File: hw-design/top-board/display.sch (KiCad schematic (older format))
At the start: 0 parts

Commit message: sch,top-board: added glcd
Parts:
- added C? (x18): 1uF, symbol C
- added C? (x2): 100nF, symbol C
- added C? (x2): 10uF, symbol CP
- added DS? (x2): ERC12864-2, symbol ERC12864-2
- added P? (x2): BACKLIGHT, symbol CONN_01X02
- added Q? (x2): 2N7002, symbol Q_NMOS_GSD
- added R? (x2): 100K, symbol R
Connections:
- new net: C?.1, DS?.10 (CAP2-) (x2)
- new net: C?.2, DS?.11 (CAP2+) (x2)
- new net: C?.1, DS?.12 (CAP1+) (x2)
- new net: C?.2, C?.2, DS?.13 (CAP1-) (x2)
- new net: C?.1, DS?.14 (CAP3+) (x2)
- new net: C?.2, DS?.15 (VOUT) (x2)
- new net: C?.2, DS?.6 (V4) (x2)
- new net: C?.2, DS?.7 (V3) (x2)
- new net: C?.2, DS?.8 (V2) (x2)
- new net: C?.2, DS?.9 (V1) (x2)
- new net: C?.2, DS?.5 (V0) (x2)
- new net: P?.1 (P1), Q?.3 (D), R?.1 (x2)
- new net +3V3: C?.1, C?.1, C?.1, C?.1, DS?.1 (IRS), DS?.1 (IRS), DS?.17 (VDD), DS?.17 (VDD), DS?.20 (DB5), DS?.20 (DB5), DS?.21 (DB4), DS?.21 (DB4), DS?.22 (DB3), DS?.22 (DB3), DS?.23 (DB2), DS?.23 (DB2), DS?.24 (DB1), DS?.24 (DB1), DS?.25 (DB0), DS?.25 (DB0), DS?.26 (~RD~(E)), DS?.26 (~RD~(E)), DS?.27 (~WR~(R~W~)), DS?.27 (~WR~(R~W~)), P?.2 (P2), P?.2 (P2), R?.2, R?.2
- new net GLCD1_BL: Q?.1 (G)
- new net GLCD1_CS: DS?.30 (~CS~)
- new net GLCD2_BL: Q?.1 (G)
- new net GLCD2_CS: DS?.30 (~CS~)
- new net GLCD_A0: DS?.28 (A0), DS?.28 (A0)
- new net GLCD_RESET: DS?.29 (~RES~), DS?.29 (~RES~)
- new net GLCD_SCL: DS?.19 (DB6(SCL)), DS?.19 (DB6(SCL))
- new net GLCD_SI: DS?.18 (DB7(SI)), DS?.18 (DB7(SI))
- new net GNDD: C?.1, C?.1, C?.1, C?.1, C?.1, C?.1, C?.1, C?.1, C?.1, C?.1, C?.1, C?.1, C?.2, C?.2, C?.2, C?.2, DS?.16 (VSS), DS?.16 (VSS), DS?.2 (P/~S~), DS?.2 (P/~S~), DS?.3 (C86), DS?.3 (C86), Q?.2 (S), Q?.2 (S)
- no-connect marks 0 -> 2

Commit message: sch,top-board: annotation done
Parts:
- gave numbers to parts that had none: 30

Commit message: sch,top-board: DRC passing
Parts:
- added R2, R4: 100R, symbol R
- renumbered R2 to R3
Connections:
- net +3V3: now also R2.2, R4.2; no longer DS1.20 (DB5), DS1.21 (DB4), DS1.22 (DB3), DS1.23 (DB2), DS1.24 (DB1), DS1.25 (DB0), DS1.26 (~RD~(E)), DS1.27 (~WR~(R~W~)), DS2.20 (DB5), DS2.21 (DB4), DS2.22 (DB3), DS2.23 (DB2), DS2.24 (DB1), DS2.25 (DB0), DS2.26 (~RD~(E)), DS2.27 (~WR~(R~W~))
- new net: DS2.20 (DB5), DS2.21 (DB4), DS2.22 (DB3), DS2.23 (DB2), DS2.24 (DB1), DS2.25 (DB0), DS2.26 (~RD~(E)), DS2.27 (~WR~(R~W~)), R4.1
- new net: DS1.20 (DB5), DS1.21 (DB4), DS1.22 (DB3), DS1.23 (DB2), DS1.24 (DB1), DS1.25 (DB0), DS1.26 (~RD~(E)), DS1.27 (~WR~(R~W~)), R2.1

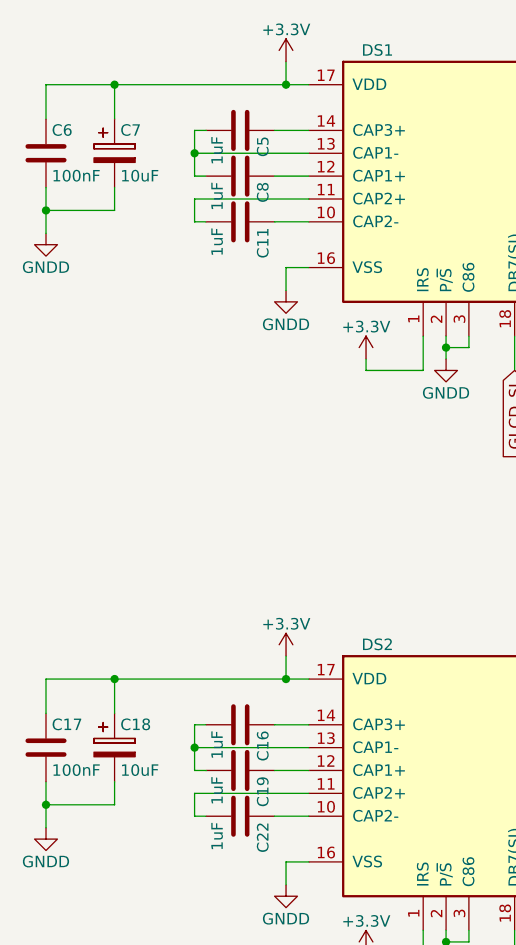
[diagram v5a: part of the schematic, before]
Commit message: sch,top-board: BOM added
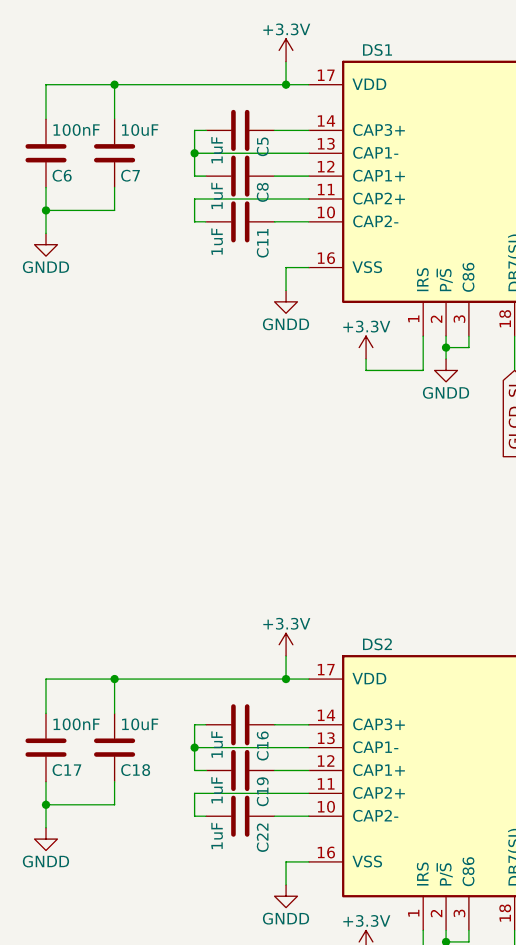
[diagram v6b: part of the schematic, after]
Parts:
- removed C18, C7: 10uF, symbol CP
- added C18, C7: 10uF, symbol C
- C10, C11, C12, C13, C14, C15, C16, C19, C20, C21, C22, C23, C24, C25, C26, C5, C8, C9: MPN (none) -> C2012X7R1E105K125AB
- C17, C6: MPN (none) -> C1608X7R1E104K080AA
- DS1, DS2: MPN (none) -> ERC12864FSF-2
- Q1, Q2: MPN (none) -> 2N7002P,215
- R1, R3: MPN (none) -> RMCF0603JT100K
- R2, R4: MPN (none) -> RMCF0603JT100R
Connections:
- net +3V3: now also C17.2, C6.2, C18.2, C7.2; no longer C17.1, C6.1
- net GNDD: now also C17.1, C6.1, C18.1, C7.1; no longer C17.2, C6.2

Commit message: sch,top-board: footprints creation/assignment done
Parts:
- C10, C11, C12, C13, C14, C15, C16, C18, C19, C20, C21, C22, C23, C24, C25, C26, C5, C7, C8, C9: footprint (none) -> Capacitors_SMD:C_0805
- C17, C6: footprint (none) -> Capacitors_SMD:C_0603
- DS1, DS2: footprint (none) -> footprints:ER-CON30HB-1
- P2: footprint (none) -> footprints:SMD_Pin_Header_Angled_2x01_Pitch2mm; MPN (none) -> ER-CON2.0-2P-SMD
- P3: MPN (none) -> footprints:SMD_Pin_Header_Angled_2x01_Pitch2mm
- Q1, Q2: footprint (none) -> Housings_SOT-23_SOT-143_TSOT-6:SOT-23
- R1, R2, R3, R4: footprint (none) -> Resistors_SMD:R_0603
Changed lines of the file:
@@
 F 0 "DS1" H 4200 2250 50  0000 C CNN
 F 1 "ERC12864-2" H 5200 2250 50  0000 C CNN
-F 2 "" H 5200 2250 50  0000 C CIN
+F 2 "footprints:ER-CON30HB-1" H 5200 2250 50  0001 C CIN
 F 3 "" H 5200 1600 60  0000 C CNN
 F 4 "ERC12864FSF-2" H 0   0   50  0001 C CNN "MPN"
@@
 F 0 "C11" H 3625 2000 50  0000 L CNN
 F 1 "1uF" H 3625 1800 50  0000 L CNN
-F 2 "" H 3638 1750 30  0000 C CNN
+F 2 "Capacitors_SMD:C_0805" H 3638 1750 30  0001 C CNN
 F 3 "" H 3600 1900 60  0000 C CNN
 F 4 "C2012X7R1E105K125AB" H 0   0   50  0001 C CNN "MPN"
@@
 F 0 "C8" H 3625 1800 50  0000 L CNN
 F 1 "1uF" H 3625 1600 50  0000 L CNN
-F 2 "" H 3638 1550 30  0000 C CNN
+F 2 "Capacitors_SMD:C_0805" H 3638 1550 30  0001 C CNN
 F 3 "" H 3600 1700 60  0000 C CNN
 F 4 "C2012X7R1E105K125AB" H 0   0   50  0001 C CNN "MPN"
@@
 F 0 "C5" H 3625 1600 50  0000 L CNN
 F 1 "1uF" H 3625 1400 50  0000 L CNN
-F 2 "" H 3638 1350 30  0000 C CNN
+F 2 "Capacitors_SMD:C_0805" H 3638 1350 30  0001 C CNN
 F 3 "" H 3600 1500 60  0000 C CNN
 F 4 "C2012X7R1E105K125AB" H 0   0   50  0001 C CNN "MPN"
@@
 F 0 "C15" H 6500 2300 50  0000 L CNN
 F 1 "1uF" H 6625 2100 50  0000 L CNN
-F 2 "" H 6638 2050 30  0000 C CNN
+F 2 "Capacitors_SMD:C_0805" H 6638 2050 30  0001 C CNN
 F 3 "" H 6600 2200 60  0000 C CNN
 F 4 "C2012X7R1E105K125AB" H 0   0   50  0001 C CNN "MPN"
@@
 F 0 "C14" H 6700 2200 50  0000 L CNN
 F 1 "1uF" H 6825 2000 50  0000 L CNN
-F 2 "" H 6838 1950 30  0000 C CNN
+F 2 "Capacitors_SMD:C_0805" H 6838 1950 30  0001 C CNN
 F 3 "" H 6800 2100 60  0000 C CNN
 F 4 "C2012X7R1E105K125AB" H 0   0   50  0001 C CNN "MPN"
@@
 F 0 "C13" H 6900 2100 50  0000 L CNN
 F 1 "1uF" H 7025 1900 50  0000 L CNN
-F 2 "" H 7038 1850 30  0000 C CNN
+F 2 "Capacitors_SMD:C_0805" H 7038 1850 30  0001 C CNN
 F 3 "" H 7000 2000 60  0000 C CNN
 F 4 "C2012X7R1E105K125AB" H 0   0   50  0001 C CNN "MPN"
@@
 F 0 "C12" H 7100 2000 50  0000 L CNN
 F 1 "1uF" H 7225 1800 50  0000 L CNN
-F 2 "" H 7238 1750 30  0000 C CNN
+F 2 "Capacitors_SMD:C_0805" H 7238 1750 30  0001 C CNN
 F 3 "" H 7200 1900 60  0000 C CNN
 F 4 "C2012X7R1E105K125AB" H 0   0   50  0001 C CNN "MPN"
@@
 F 0 "C10" H 7300 1900 50  0000 L CNN
 F 1 "1uF" H 7425 1700 50  0000 L CNN
-F 2 "" H 7438 1650 30  0000 C CNN
+F 2 "Capacitors_SMD:C_0805" H 7438 1650 30  0001 C CNN
 F 3 "" H 7400 1800 60  0000 C CNN
 F 4 "C2012X7R1E105K125AB" H 0   0   50  0001 C CNN "MPN"
@@
 F 0 "C9" H 7500 1800 50  0000 L CNN
 F 1 "1uF" H 7625 1600 50  0000 L CNN
-F 2 "" H 7638 1550 30  0000 C CNN
+F 2 "Capacitors_SMD:C_0805" H 7638 1550 30  0001 C CNN
 F 3 "" H 7600 1700 60  0000 C CNN
 F 4 "C2012X7R1E105K125AB" H 0   0   50  0001 C CNN "MPN"
@@
 F 0 "C6" H 2775 1700 50  0000 L CNN
 F 1 "100nF" H 2775 1500 50  0000 L CNN
-F 2 "" H 2788 1450 30  0000 C CNN
+F 2 "Capacitors_SMD:C_0603" H 2788 1450 30  0001 C CNN
 F 3 "" H 2750 1600 60  0000 C CNN
 F 4 "C1608X7R1E104K080AA" H 0   0   50  0001 C CNN "MPN"
@@
 F 0 "DS2" H 4200 4850 50  0000 C CNN
 F 1 "ERC12864-2" H 5200 4850 50  0000 C CNN
-F 2 "" H 5200 4850 50  0000 C CIN
+F 2 "footprints:ER-CON30HB-1" H 5200 4850 50  0001 C CIN
 F 3 "" H 5200 4200 60  0000 C CNN
 F 4 "ERC12864FSF-2" H 0   0   50  0001 C CNN "MPN"
@@
 F 0 "C22" H 3625 4600 50  0000 L CNN
 F 1 "1uF" H 3625 4400 50  0000 L CNN
-F 2 "" H 3638 4350 30  0000 C CNN
+F 2 "Capacitors_SMD:C_0805" H 3638 4350 30  0001 C CNN
 F 3 "" H 3600 4500 60  0000 C CNN
 F 4 "C2012X7R1E105K125AB" H 0   0   50  0001 C CNN "MPN"
@@
 F 0 "C19" H 3625 4400 50  0000 L CNN
 F 1 "1uF" H 3625 4200 50  0000 L CNN
-F 2 "" H 3638 4150 30  0000 C CNN
+F 2 "Capacitors_SMD:C_0805" H 3638 4150 30  0001 C CNN
 F 3 "" H 3600 4300 60  0000 C CNN
 F 4 "C2012X7R1E105K125AB" H 0   0   50  0001 C CNN "MPN"
@@
 F 0 "C16" H 3625 4200 50  0000 L CNN
 F 1 "1uF" H 3625 4000 50  0000 L CNN
-F 2 "" H 3638 3950 30  0000 C CNN
+F 2 "Capacitors_SMD:C_0805" H 3638 3950 30  0001 C CNN
 F 3 "" H 3600 4100 60  0000 C CNN
 F 4 "C2012X7R1E105K125AB" H 0   0   50  0001 C CNN "MPN"
@@
 F 0 "C26" H 6500 4900 50  0000 L CNN
 F 1 "1uF" H 6625 4700 50  0000 L CNN
-F 2 "" H 6638 4650 30  0000 C CNN
+F 2 "Capacitors_SMD:C_0805" H 6638 4650 30  0001 C CNN
 F 3 "" H 6600 4800 60  0000 C CNN
 F 4 "C2012X7R1E105K125AB" H 0   0   50  0001 C CNN "MPN"
@@
 F 0 "C25" H 6700 4800 50  0000 L CNN
 F 1 "1uF" H 6825 4600 50  0000 L CNN
-F 2 "" H 6838 4550 30  0000 C CNN
+F 2 "Capacitors_SMD:C_0805" H 6838 4550 30  0001 C CNN
 F 3 "" H 6800 4700 60  0000 C CNN
 F 4 "C2012X7R1E105K125AB" H 0   0   50  0001 C CNN "MPN"
@@
 F 0 "C24" H 6900 4700 50  0000 L CNN
 F 1 "1uF" H 7025 4500 50  0000 L CNN
-F 2 "" H 7038 4450 30  0000 C CNN
+F 2 "Capacitors_SMD:C_0805" H 7038 4450 30  0001 C CNN
 F 3 "" H 7000 4600 60  0000 C CNN
 F 4 "C2012X7R1E105K125AB" H 0   0   50  0001 C CNN "MPN"
@@
 F 0 "C23" H 7100 4600 50  0000 L CNN
 F 1 "1uF" H 7225 4400 50  0000 L CNN
-F 2 "" H 7238 4350 30  0000 C CNN
+F 2 "Capacitors_SMD:C_0805" H 7238 4350 30  0001 C CNN
 F 3 "" H 7200 4500 60  0000 C CNN
 F 4 "C2012X7R1E105K125AB" H 0   0   50  0001 C CNN "MPN"
@@
 F 0 "C21" H 7300 4500 50  0000 L CNN
 F 1 "1uF" H 7425 4300 50  0000 L CNN
-F 2 "" H 7438 4250 30  0000 C CNN
+F 2 "Capacitors_SMD:C_0805" H 7438 4250 30  0001 C CNN
 F 3 "" H 7400 4400 60  0000 C CNN
 F 4 "C2012X7R1E105K125AB" H 0   0   50  0001 C CNN "MPN"
@@
 F 0 "C20" H 7500 4400 50  0000 L CNN
 F 1 "1uF" H 7625 4200 50  0000 L CNN
-F 2 "" H 7638 4150 30  0000 C CNN
+F 2 "Capacitors_SMD:C_0805" H 7638 4150 30  0001 C CNN
 F 3 "" H 7600 4300 60  0000 C CNN
 F 4 "C2012X7R1E105K125AB" H 0   0   50  0001 C CNN "MPN"
@@
 F 0 "P2" H 9250 1550 50  0000 C CNN
 F 1 "BACKLIGHT" V 9350 1400 50  0000 C CNN
-F 2 "" H 9250 1400 60  0000 C CNN
+F 2 "footprints:SMD_Pin_Header_Angled_2x01_Pitch2mm" H 9250 1400 60  0001 C CNN
 F 3 "" H 9250 1400 60  0000 C CNN
+F 4 "ER-CON2.0-2P-SMD" H 9250 1400 60  0001 C CNN "MPN"
 	1    9250 1400
 	0    -1   -1   0
@@
 F 0 "R1" V 8980 1500 50  0000 C CNN
 F 1 "100K" V 8900 1500 50  0000 C CNN
-F 2 "" V 8830 1500 30  0000 C CNN
+F 2 "Resistors_SMD:R_0603" V 8830 1500 30  0001 C CNN
 F 3 "" H 8900 1500 30  0000 C CNN
 F 4 "RMCF0603JT100K" H 0   0   50  0001 C CNN "MPN"
@@
 F 0 "P3" H 9250 4150 50  0000 C CNN
 F 1 "BACKLIGHT" V 9350 4000 50  0000 C CNN
-F 2 "" H 9250 4000 60  0000 C CNN
+F 2 "" H 9250 4000 60  0001 C CNN
 F 3 "" H 9250 4000 60  0000 C CNN
+F 4 "ER-CON2.0-2P-SMD" H 9250 4000 60  0001 C CNN "MPN"
+F 5 "footprints:SMD_Pin_Header_Angled_2x01_Pitch2mm" H 9250 4000 60  0001 C CNN "MPN"
 	1    9250 4000
 	0    -1   -1   0
@@
 F 0 "R3" V 8980 4100 50  0000 C CNN
 F 1 "100K" V 8900 4100 50  0000 C CNN
-F 2 "" V 8830 4100 30  0000 C CNN
+F 2 "Resistors_SMD:R_0603" V 8830 4100 30  0001 C CNN
 F 3 "" H 8900 4100 30  0000 C CNN
 F 4 "RMCF0603JT100K" H 0   0   50  0001 C CNN "MPN"
@@
 F 0 "Q1" H 9400 2100 50  0000 R CNN
 F 1 "2N7002" H 9600 2000 50  0000 R CNN
-F 2 "" H 9300 2150 29  0000 C CNN
+F 2 "Housings_SOT-23_SOT-143_TSOT-6:SOT-23" H 9300 2150 29  0001 C CNN
 F 3 "" H 9100 2050 60  0000 C CNN
 F 4 "2N7002P,215" H 0   0   50  0001 C CNN "MPN"
@@
 F 0 "Q2" H 9400 4700 50  0000 R CNN
 F 1 "2N7002" H 9600 4600 50  0000 R CNN
-F 2 "" H 9300 4750 29  0000 C CNN
+F 2 "Housings_SOT-23_SOT-143_TSOT-6:SOT-23" H 9300 4750 29  0001 C CNN
 F 3 "" H 9100 4650 60  0000 C CNN
 F 4 "2N7002P,215" H 0   0   50  0001 C CNN "MPN"
@@
 F 0 "R4" V 5680 5450 50  0000 C CNN
 F 1 "100R" V 5600 5450 50  0000 C CNN
-F 2 "" V 5530 5450 30  0000 C CNN
+F 2 "Resistors_SMD:R_0603" V 5530 5450 30  0001 C CNN
 F 3 "" H 5600 5450 30  0000 C CNN
 F 4 "RMCF0603JT100R" H 0   0   50  0001 C CNN "MPN"
@@
 F 0 "R2" V 5680 2850 50  0000 C CNN
 F 1 "100R" V 5600 2850 50  0000 C CNN
-F 2 "" V 5530 2850 30  0000 C CNN
+F 2 "Resistors_SMD:R_0603" V 5530 2850 30  0001 C CNN
 F 3 "" H 5600 2850 30  0000 C CNN
 F 4 "RMCF0603JT100R" H 0   0   50  0001 C CNN "MPN"
@@
 F 0 "C7" H 3075 1700 50  0000 L CNN
 F 1 "10uF" H 3075 1500 50  0000 L CNN
-F 2 "" H 3088 1450 30  0000 C CNN
+F 2 "Capacitors_SMD:C_0805" H 3088 1450 30  0001 C CNN
 F 3 "" H 3050 1600 60  0000 C CNN
 F 4 "GRM219R61E106KA12D" H 300 0   50  0001 C CNN "MPN"
@@
 F 0 "C18" H 3075 4300 50  0000 L CNN
 F 1 "10uF" H 3075 4100 50  0000 L CNN
-F 2 "" H 3088 4050 30  0000 C CNN
+F 2 "Capacitors_SMD:C_0805" H 3088 4050 30  0001 C CNN
 F 3 "" H 3050 4200 60  0000 C CNN
 F 4 "GRM219R61E106KA12D" H 300 2600 50  0001 C CNN "MPN"
@@
 F 0 "C17" H 2775 4300 50  0000 L CNN
 F 1 "100nF" H 2775 4100 50  0000 L CNN
-F 2 "" H 2788 4050 30  0000 C CNN
+F 2 "Capacitors_SMD:C_0603" H 2788 4050 30  0001 C CNN
 F 3 "" H 2750 4200 60  0000 C CNN
 F 4 "C1608X7R1E104K080AA" H 0   2600 50  0001 C CNN "MPN"

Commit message: sch,top-board: fix footprint name of the LCD power conn
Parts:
- P2: footprint footprints:SMD_Pin_Header_Angled_2x01_Pitch2mm -> Pin_Headers:SMD_Pin_Header_Angled_2x01_Pitch2.00mm
- P3: footprint (none) -> Pin_Headers:SMD_Pin_Header_Angled_2x01_Pitch2.00mm; MPN footprints:SMD_Pin_Header_Angled_2x01_Pitch2mm -> ER-CON2.0-2P-SMD
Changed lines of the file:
@@
 F 0 "P2" H 9250 1550 50  0000 C CNN
 F 1 "BACKLIGHT" V 9350 1400 50  0000 C CNN
-F 2 "footprints:SMD_Pin_Header_Angled_2x01_Pitch2mm" H 9250 1400 60  0001 C CNN
+F 2 "Pin_Headers:SMD_Pin_Header_Angled_2x01_Pitch2.00mm" H 9250 1400 60  0001 C CNN
 F 3 "" H 9250 1400 60  0000 C CNN
 F 4 "ER-CON2.0-2P-SMD" H 9250 1400 60  0001 C CNN "MPN"
@@
 F 0 "P3" H 9250 4150 50  0000 C CNN
 F 1 "BACKLIGHT" V 9350 4000 50  0000 C CNN
-F 2 "" H 9250 4000 60  0001 C CNN
+F 2 "Pin_Headers:SMD_Pin_Header_Angled_2x01_Pitch2.00mm" H 9250 4000 60  0001 C CNN
 F 3 "" H 9250 4000 60  0000 C CNN
 F 4 "ER-CON2.0-2P-SMD" H 9250 4000 60  0001 C CNN "MPN"
-F 5 "footprints:SMD_Pin_Header_Angled_2x01_Pitch2mm" H 9250 4000 60  0001 C CNN "MPN"
 	1    9250 4000
 	0    -1   -1   0
